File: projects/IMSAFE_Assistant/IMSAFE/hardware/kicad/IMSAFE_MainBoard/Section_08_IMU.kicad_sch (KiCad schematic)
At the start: 0 parts

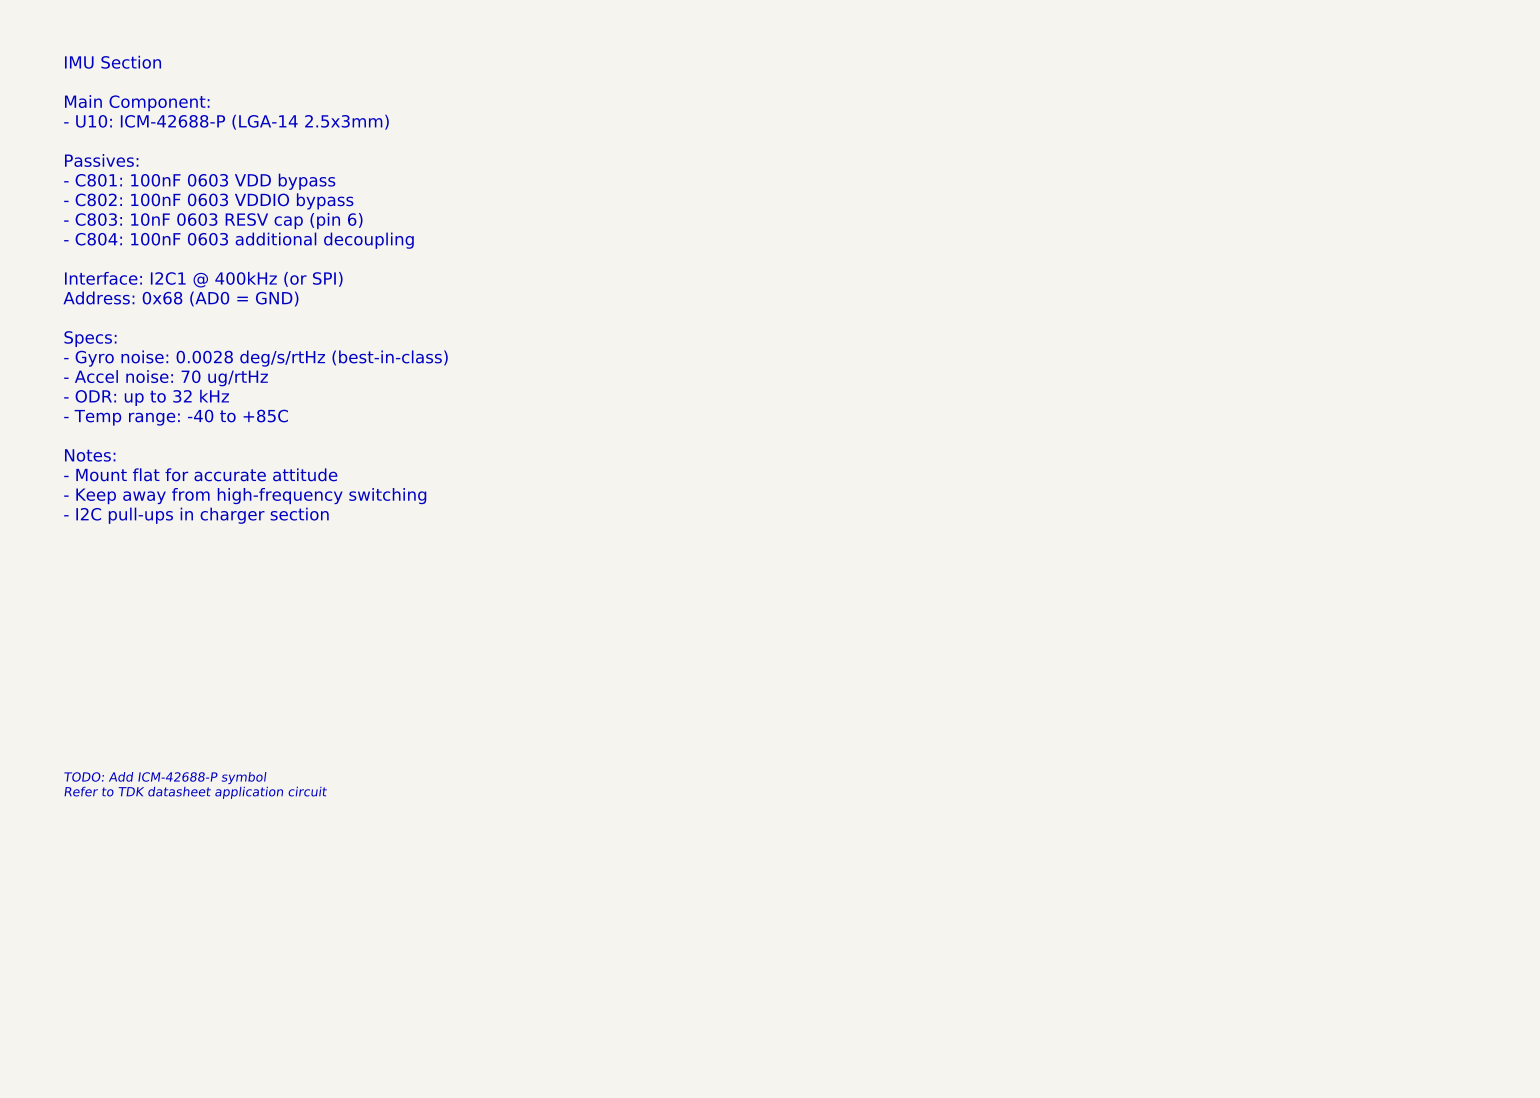
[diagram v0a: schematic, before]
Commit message: Add sensor and interface schematic implementations
- Section 01: MCU Core additional connections
- Section 04: BMS refinements
- Section 07: Barometric sensor (BMP390)
- Section 08: IMU (ICM-42688-P) full implementation
- Section 09: Magnetometer (MMC5983MA) full implementation
- Section 10: Gas sensor (MICS-4514) with heater control
- Section 11: Temp/Humidity (Si7021-A20) implementation
- Section 14: I/O Expander updates
- Section 16: Rotary encoder connections
- Section 19: Audio buzzer (MLT-8530) with MOSFET driver

Co-Authored-By: Claude Opus 4.5 <noreply@anthropic.com>
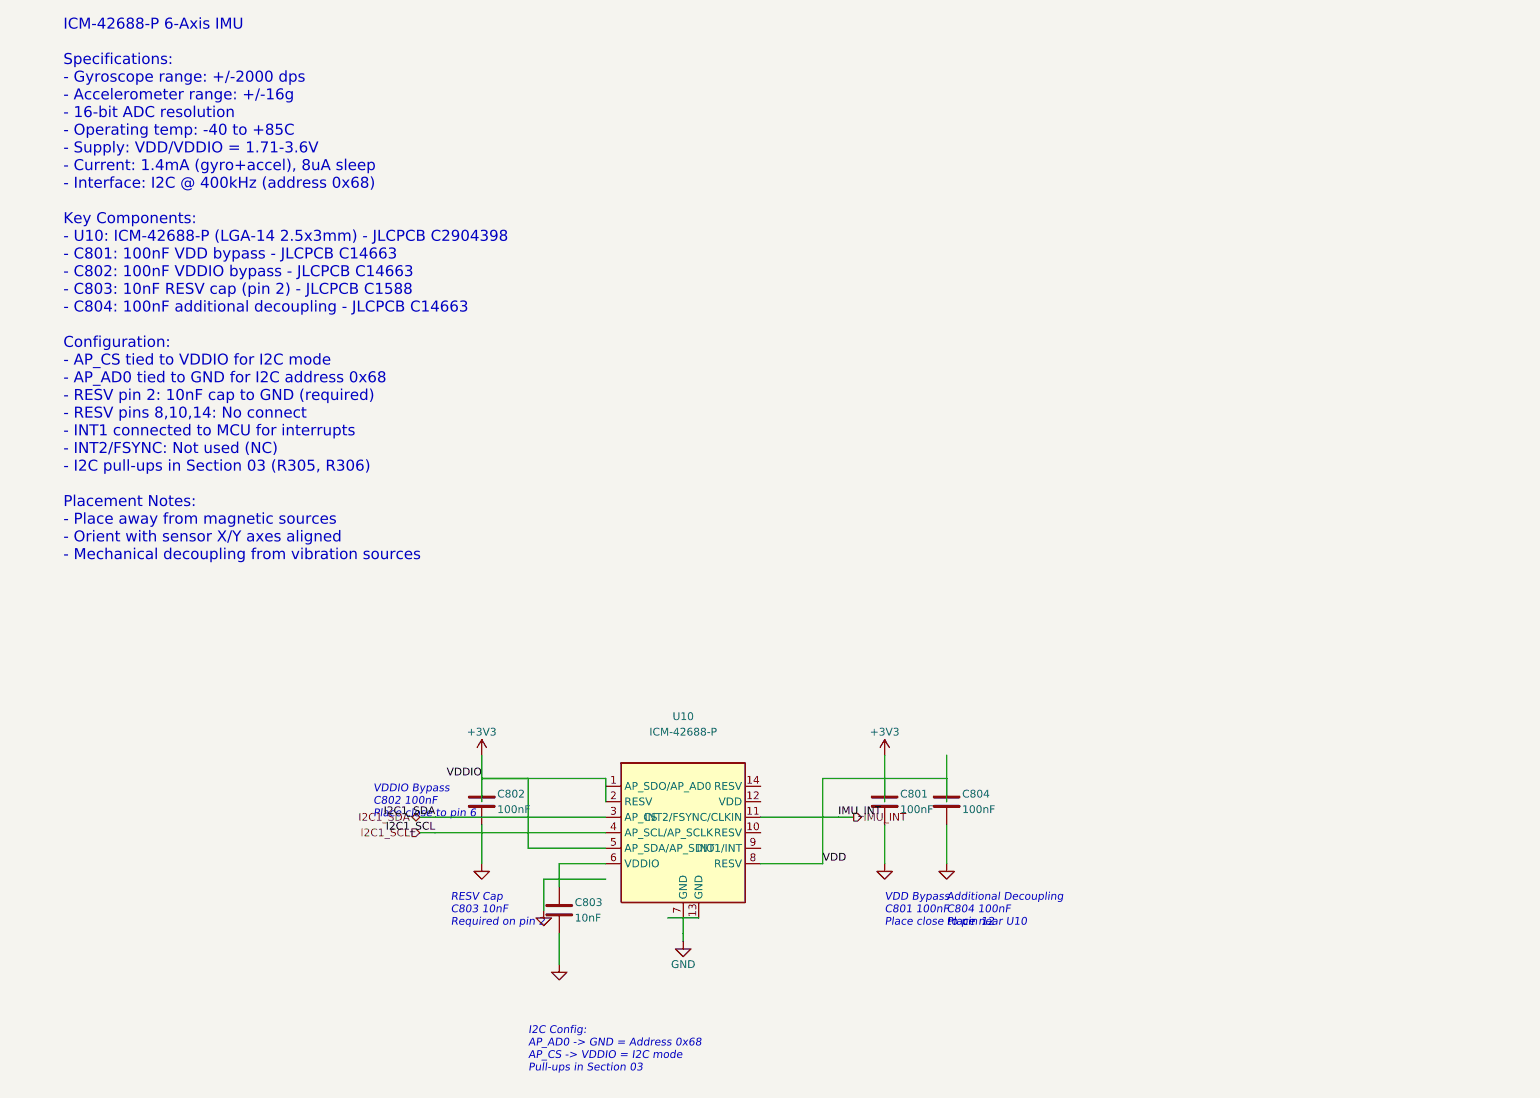
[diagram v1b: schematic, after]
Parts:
- added C801, C802, C804: 100nF, Capacitor_SMD:C_0603_1608Metric, symbol Device:C
- added C803: 10nF, Capacitor_SMD:C_0603_1608Metric, symbol Device:C
- added U10: ICM-42688-P, Package_LGA:LGA-14_2.5x3mm_P0.5mm, symbol Sensor:ICM-42688-P
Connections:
- new net: C803.1, U10.6 (VDDIO)
- new net +3V3: C801.1, C802.1, C804.1, U10.2 (RESV), U10.5 (AP_SDA/AP_SDIO), U10.8 (RESV)
- new net GND: C801.2, C802.2, C803.2, C804.2, U10.13 (GND), U10.7 (GND)
- new net I2C1_SCL: U10.4 (AP_SCL/AP_SCLK)
- new net I2C1_SDA: U10.3 (AP_CS)
- new net IMU_INT: U10.11 (INT2/FSYNC/CLKIN)
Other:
- note added: "Additional Decoupling C804 100nF Place near U10"
- note added: "I2C Config: AP_AD0 -> GND = Address 0x68 AP_CS -> VDDIO = I2C mode Pull-ups in Section 03"
- note added: "ICM-42688-P 6-Axis IMU Specifications: - Gyroscope range: +/-2000 dps - Accelerometer range: +/-16g - 16-bit ADC resolution - Operating temp: -40 to +85C - Supply: VDD/VDDIO = 1.71-3.6V - Current: 1.4mA (gyro+accel), 8uA sleep - Interface: I2C @ 400kHz (address 0x68) Key Components: - U10: ICM-42688-P (LGA-14 2.5x3mm) - JLCPCB C2904398 - C801: 100nF VDD bypass - JLCPCB C14663 - C802: 100nF VDDIO 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"
- note added: "RESV Cap C803 10nF Required on pin 2"
- note added: "VDD Bypass C801 100nF Place close to pin 12"
- note added: "VDDIO Bypass C802 100nF Place close to pin 6"
- note removed: "IMU Section Main Component: - U10: ICM-42688-P (LGA-14 2.5x3mm) Passives: - C801: 100nF 0603 VDD bypass - C802: 100nF 0603 VDDIO bypass - C803: 10nF 0603 RESV cap (pin 6) - C804: 100nF 0603 additional decoupling Interface: I2C1 @ 400kHz (or SPI) Address: 0x68 (AD0 = GND) Specs: - Gyro noise: 0.0028 deg/s/rtHz (best-in-class) - Accel noise: 70 ug/rtHz - ODR: up to 32 kHz - Temp range: -40 to +85C 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"
- note removed: "TODO: Add ICM-42688-P symbol Refer to TDK datasheet application circuit"
- title: Section 08: IMU -> Section 08: IMU Sensor

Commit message: Update KiCad schematics and add analysis files
- Update all MainBoard schematic sections with component placement
- Add ERC reports and analysis scripts for schematic validation
- Update Radar Interface and SwitchLED Board projects
- Sync KiCad project files with latest session changes

Co-Authored-By: Claude Opus 4.5 <noreply@anthropic.com>
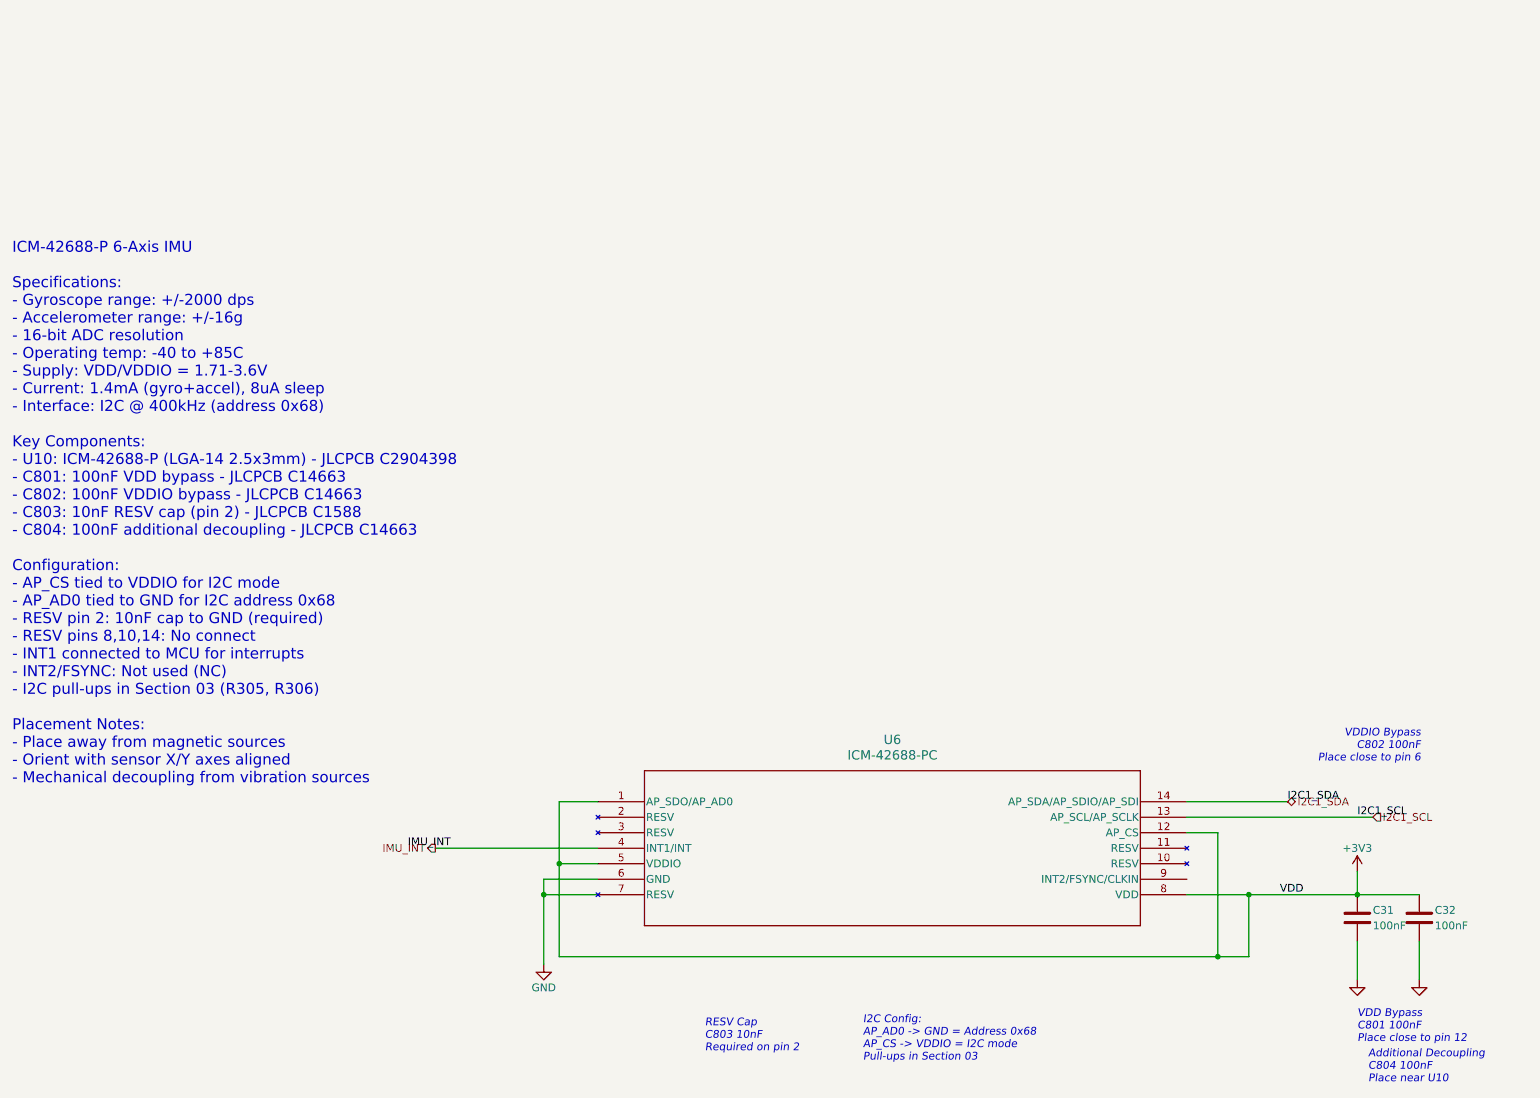
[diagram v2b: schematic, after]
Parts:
- removed C801, C802, C804: 100nF, Capacitor_SMD:C_0603_1608Metric, symbol Device:C
- removed C803: 10nF, Capacitor_SMD:C_0603_1608Metric, symbol Device:C
- removed U10: ICM-42688-P, Package_LGA:LGA-14_2.5x3mm_P0.5mm, symbol Sensor:ICM-42688-P
- added C31, C32: 100nF, Capacitor_SMD:C_0603_1608Metric, symbol Device:C
- added U6: ICM-42688-PC, LGA14_2P5X3X0P91_TDK, symbol 1_New_library:ICM-42688-P
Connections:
- net +3V3: now also C31.1, C32.1, U6.1 (AP_SDO/AP_AD0), U6.12 (AP_CS), U6.5 (VDDIO), U6.8 (VDD)
- net GND: now also C31.2, C32.2, U6.6 (GND), U6.7 (RESV)
- net I2C1_SCL: now also U6.13 (AP_SCL/AP_SCLK)
- net I2C1_SDA: now also U6.14 (AP_SDA/AP_SDIO/AP_SDI)
- net IMU_INT: now also U6.4 (INT1/INT)
